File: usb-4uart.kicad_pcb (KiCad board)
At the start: 2 copper layers, 25 x 65 mm, 53 parts, among them J1 Conn_02x05_Odd_Even, X1 24MHz

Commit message: updated a bit
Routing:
- net USB_IN-: track 10.3 -> 10.8 mm
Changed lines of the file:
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@@
 	)
 	(segment
-		(start 49 86.25)
-		(end 49 78.8)
-		(width 0.4)
+		(start 34.396225 78.096225)
+		(end 34.8 78.5)
+		(width 0.2)
 		(layer "F.Cu")
 		(net 3)
 	)
 	(segment
-		(start 34.396225 78.096225)
-		(end 34.8 78.5)
-		(width 0.2)
+		(start 49 86)
+		(end 49 78.8)
+		(width 0.4)
 		(layer "F.Cu")
 		(net 3)
@@
 	)
 	(segment
-		(start 48.75 86.25)
-		(end 49 86.25)
-		(width 0.4)
-		(layer "F.Cu")
-		(net 3)
-	)
-	(segment
 		(start 48.01 40.5)
 		(end 48.7 40.5)
@@
 	)
 	(segment
+		(start 48.75 86.25)
+		(end 49 86)
+		(width 0.4)
+		(layer "F.Cu")
+		(net 3)
+	)
+	(segment
 		(start 45 75.9)
 		(end 45.4 76.3)
@@
 	)
 	(segment
-		(start 37.15 36.531802)
-		(end 35.025 38.656802)
-		(width 0.2)
-		(layer "F.Cu")
-		(net 32)
-	)
-	(segment
-		(start 37.15 35.890001)
-		(end 37.15 36.531802)
-		(width 0.2)
-		(layer "F.Cu")
-		(net 32)
-	)
-	(segment
-		(start 35.025 41.593198)
-		(end 35.906802 42.475)
+		(start 36.75 35.01)
+		(end 36.75 36.931802)
 		(width 0.2)
 		(layer "F.Cu")
@@
 	)
 	(segment
-		(start 35.906802 42.475)
-		(end 37.453 42.475)
+		(start 36.75 36.931802)
+		(end 34.3 39.381802)
 		(width 0.2)
 		(layer "F.Cu")
@@
 	)
 	(segment
-		(start 36.75 35.01)
-		(end 36.75 35.490001)
+		(start 37.478 42.5)
+		(end 38.028 42.5)
 		(width 0.2)
 		(layer "F.Cu")
@@
 	)
 	(segment
-		(start 37.478 42.5)
-		(end 38.028 42.5)
+		(start 35.906802 42.475)
+		(end 37.453 42.475)
 		(width 0.2)
 		(layer "F.Cu")
@@
 	)
 	(segment
-		(start 35.025 38.656802)
-		(end 35.025 41.593198)
+		(start 34.3 39.381802)
+		(end 34.3 40.868198)
 		(width 0.2)
 		(layer "F.Cu")
@@
 	)
 	(segment
-		(start 36.75 35.490001)
-		(end 37.15 35.890001)
+		(start 34.3 40.868198)
+		(end 35.906802 42.475)
 		(width 0.2)
 		(layer "F.Cu")
@@
 	)
 	(segment
-		(start 38 35.01)
-		(end 38 35.490001)
+		(start 35.475 40.74711)
+		(end 35.475 40.9)
 		(width 0.2)
 		(layer "F.Cu")
@@
 	)
 	(segment
-		(start 35.475 38.843198)
-		(end 35.475 41.406802)
+		(start 35.239 39.80311)
+		(end 35.231 39.80311)
 		(width 0.2)
 		(layer "F.Cu")
@@
 	)
 	(segment
-		(start 37.453 42.025)
-		(end 37.478 42)
+		(start 35.475 40.62911)
+		(end 35.475 40.74711)
 		(width 0.2)
 		(layer "F.Cu")
@@
 	)
 	(segment
-		(start 36.093198 42.025)
-		(end 37.453 42.025)
+		(start 34.995 40.03911)
+		(end 34.995 40.15711)
 		(width 0.2)
 		(layer "F.Cu")
@@
 	)
 	(segment
-		(start 37.6 35.890001)
-		(end 37.6 36.718198)
+		(start 35.475 38.843198)
+		(end 35.475 39.56711)
 		(width 0.2)
 		(layer "F.Cu")
@@
 	)
 	(segment
-		(start 35.475 41.406802)
-		(end 36.093198 42.025)
+		(start 35.231 40.39311)
+		(end 35.239 40.39311)
 		(width 0.2)
 		(layer "F.Cu")
@@
 	)
 	(segment
-		(start 38 35.490001)
-		(end 37.6 35.890001)
+		(start 35.475 40.9)
+		(end 35.475 41.406802)
+		(width 0.2)
+		(layer "F.Cu")
+		(net 41)
+	)
+	(segment
+		(start 38 35.7)
+		(end 37.6 36.1)
+		(width 0.2)
+		(layer "F.Cu")
+		(net 41)
+	)
+	(segment
+		(start 35.475 41.406802)
+		(end 36.093198 42.025)
+		(width 0.2)
+		(layer "F.Cu")
+		(net 41)
+	)
+	(segment
+		(start 36.093198 42.025)
+		(end 37.453 42.025)
+		(width 0.2)
+		(layer "F.Cu")
+		(net 41)
+	)
+	(segment
+		(start 37.453 42.025)
+		(end 37.478 42)
+		(width 0.2)
+		(layer "F.Cu")
+		(net 41)
+	)
+	(segment
+		(start 37.6 36.1)
+		(end 37.6 36.718198)
+		(width 0.2)
+		(layer "F.Cu")
+		(net 41)
+	)
+	(segment
+		(start 38 35.01)
+		(end 38 35.7)
+		(width 0.2)
+		(layer "F.Cu")
+		(net 41)
+	)
+	(arc
+		(start 34.995 40.15711)
+		(mid 35.064123 40.323987)
+		(end 35.231 40.39311)
+		(width 0.2)
+		(layer "F.Cu")
+		(net 41)
+	)
+	(arc
+		(start 35.231 39.80311)
+		(mid 35.064123 39.872233)
+		(end 34.995 40.03911)
+		(width 0.2)
+		(layer "F.Cu")
+		(net 41)
+	)
+	(arc
+		(start 35.475 39.56711)
+		(mid 35.405877 39.733987)
+		(end 35.239 39.80311)
+		(width 0.2)
+		(layer "F.Cu")
+		(net 41)
+	)
+	(arc
+		(start 35.239 40.39311)
+		(mid 35.405877 40.462233)
+		(end 35.475 40.62911)
 		(width 0.2)
 		(layer "F.Cu")
@@
 		)
 	)
+	(generated
+		(type tuning_pattern)
+		(name "Tuning Pattern")
+		(layer "F.Cu")
+		(base_line
+			(pts
+				(xy 35.475 39.56711) (xy 35.475 40.9)
+			)
+		)
+		(corner_radius_percent 80)
+		(end
+			(xy 35.475 40.9)
+		)
+		(initial_side "right")
+		(last_diff_pair_gap 0.18)
+		(last_netname "USB_IN-")
+		(last_status "tuned")
+		(last_track_width 0.2)
+		(last_tuning "10.8169 mm (tuned)")
+		(max_amplitude 0.48)
+		(min_amplitude 0.2)
+		(min_spacing 0.59)
+		(origin
+			(xy 35.475 39.56711)
+		)
+		(override_custom_rules no)
+		(rounded yes)
+		(single_sided no)
+		(target_length 1000000)
+		(target_length_max 1000000)
+		(target_length_min 0)
+		(target_skew 0)
+		(target_skew_max 0.1)
+		(target_skew_min -0.1)
+		(tuning_mode "single")
+		(members "0181d8f1-31d1-4395-84d1-ee8fb94d2c43" "2750e0e0-310e-46a1-bdb1-e19bc1968f1a"
+			"3e03b034-2381-43cd-970a-799568e37df4" "5a4dd674-fa02-4497-860b-401a2a740b16"
+			"606ba045-15fe-4de8-9880-b822548af470" "ba59f16a-3f44-498a-a070-3c16fd823c45"
+			"cb1d8e56-2614-43b0-8465-8e681f9d9859" "f641065f-6d0c-43f3-bf87-6dc8641d3c47"
+			"fd138424-fb5d-415f-8517-59953004663c"
+		)
+	)

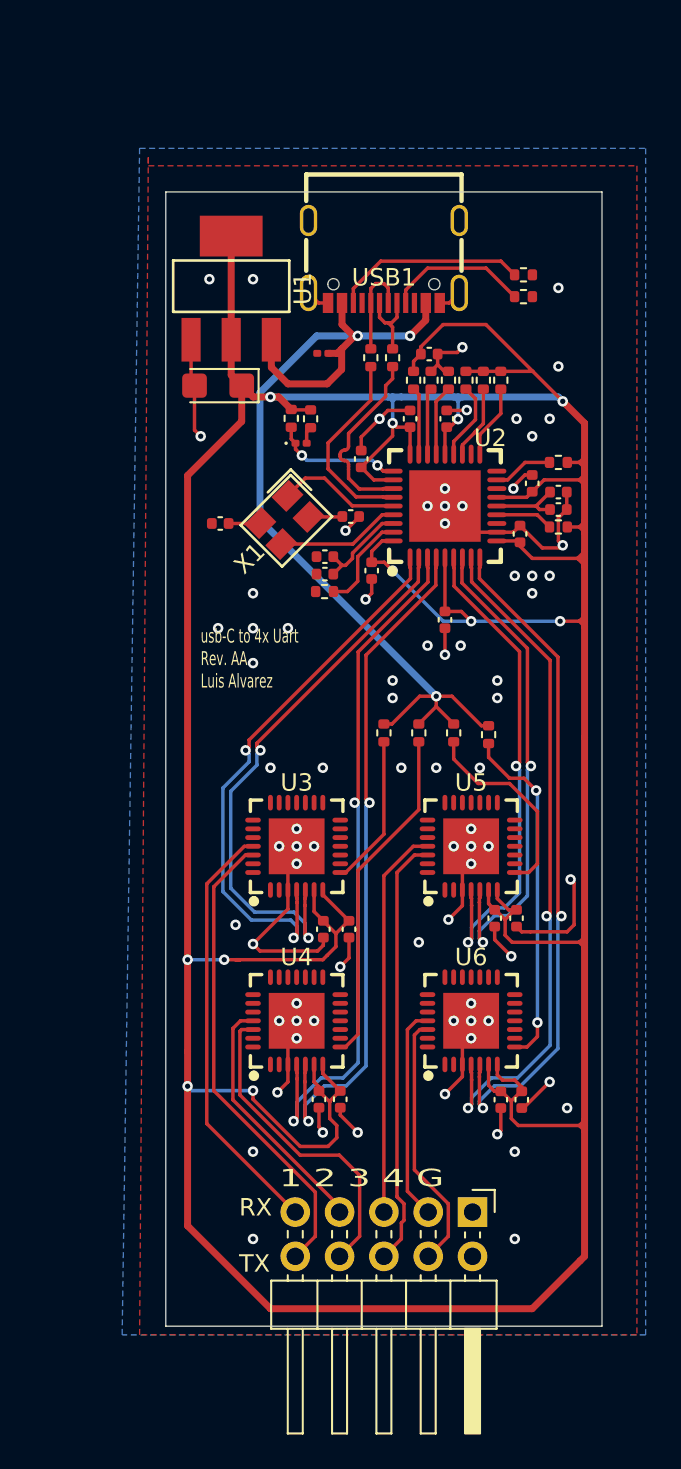
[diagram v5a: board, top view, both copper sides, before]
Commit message: updated bom and clock
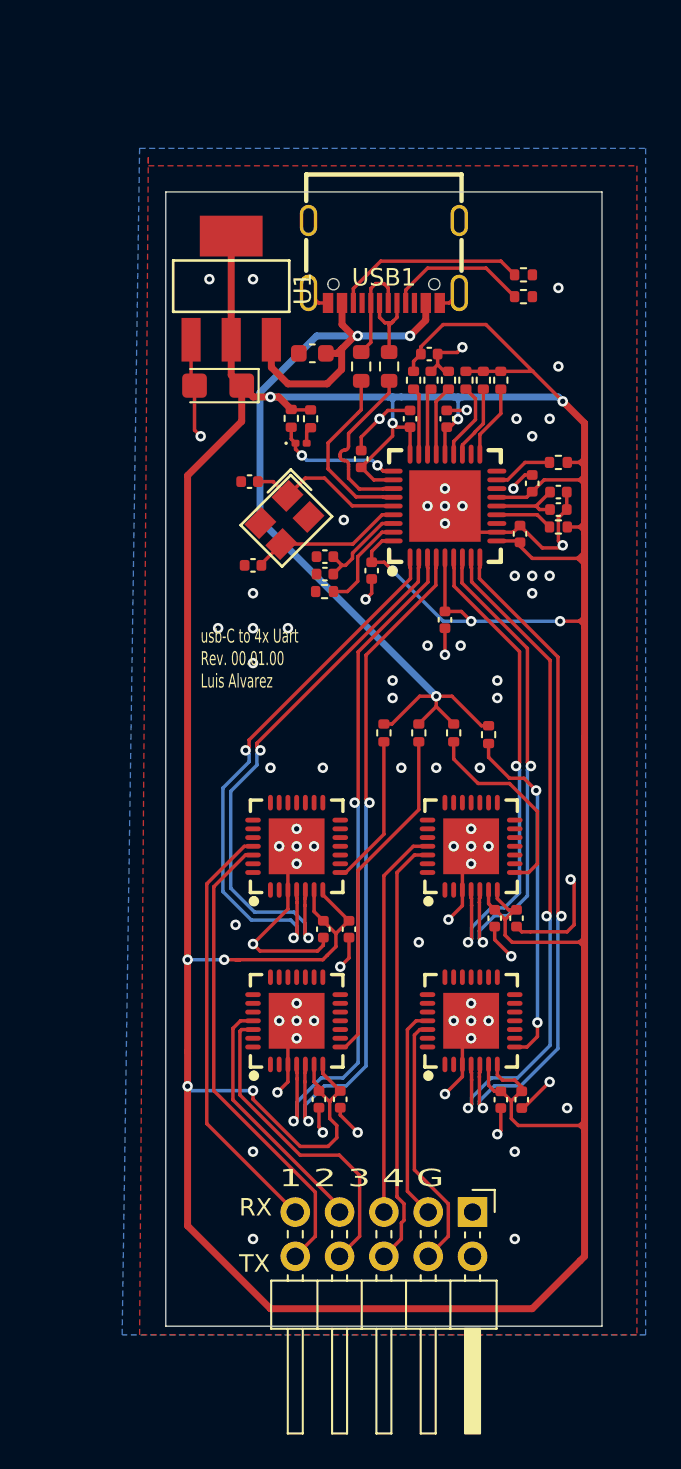
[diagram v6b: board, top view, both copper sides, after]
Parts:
- C1: footprint Capacitor_SMD:C_0201_0603Metric -> Capacitor_SMD:C_0603_1608Metric
- C6, C7: value 12pF -> 10pF
- R15, R16: footprint Resistor_SMD:R_0402_1005Metric -> Resistor_SMD:R_0603_1608Metric
- moved C7 6.14 mm to (29.8, 41.6), turned to 180 degrees
- moved C6 3.05 mm to (30.0, 46.4)
- moved R15 0.74 mm to (36.2, 35.0)
- moved C1 0.60 mm to (33.4, 34.2)
- moved R16 0.54 mm to (37.8, 35.0)
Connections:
- C6 pad 1: Net-(C6-Pad1) -> XTAL_IN
- C7 pad 1: Net-(C7-Pad1) -> XTAL_OUT
- X1 pad 2: Net-(C6-Pad1) -> GND
- X1 pad 4: Net-(C7-Pad1) -> GND
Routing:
- net XTAL_OUT: track 7.14 -> 9.17 mm
- net Net-(C7-Pad1): track 1.95 -> 0.00 mm
- net Net-(C6-Pad1): track 1.83 -> 0.00 mm
- net XTAL_IN: track 7.10 -> 8.79 mm
- net GND: track 77.7 -> 76.6 mm
- net USB_IN+: track 11.3 -> 10.2 mm
- net USB_IN-: track 10.8 -> 9.88 mm
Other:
- board text added: "usb-C to 4x Uart Rev. 00.01.00 Luis Alvarez"
- board text removed: "usb-C to 4x Uart Rev. AA Luis Alvarez"
